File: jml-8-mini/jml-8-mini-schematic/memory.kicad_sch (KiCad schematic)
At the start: 2 parts, among them U2 28HC64, U3 60L256

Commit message: lots of updates to schematic to make pcb routing easier, start on pcb design
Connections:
- net A13: now also U3.26 (NC); no longer U3.28 (VCC)
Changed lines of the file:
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@@
     (pin "25")
+    (pin "26")
     (pin "26")
     (pin "27")
     (pin "28")
-    (pin "28")
     (pin "3")

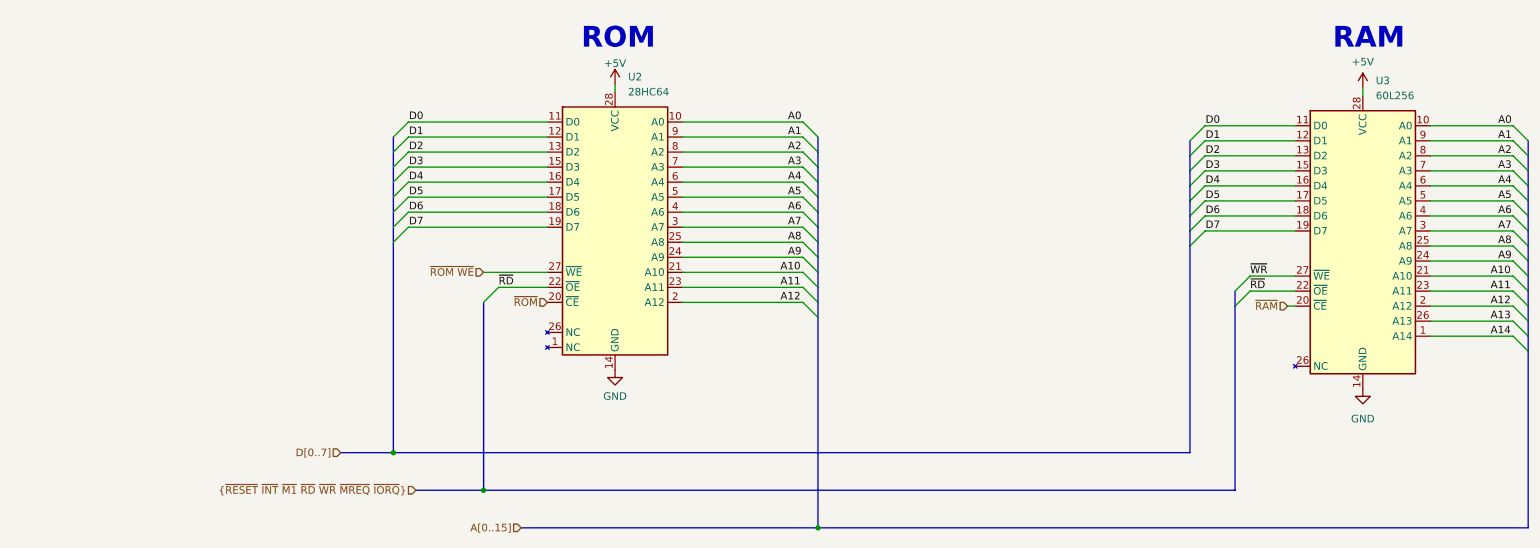
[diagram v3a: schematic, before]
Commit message: fix some errors in schematic/pcb
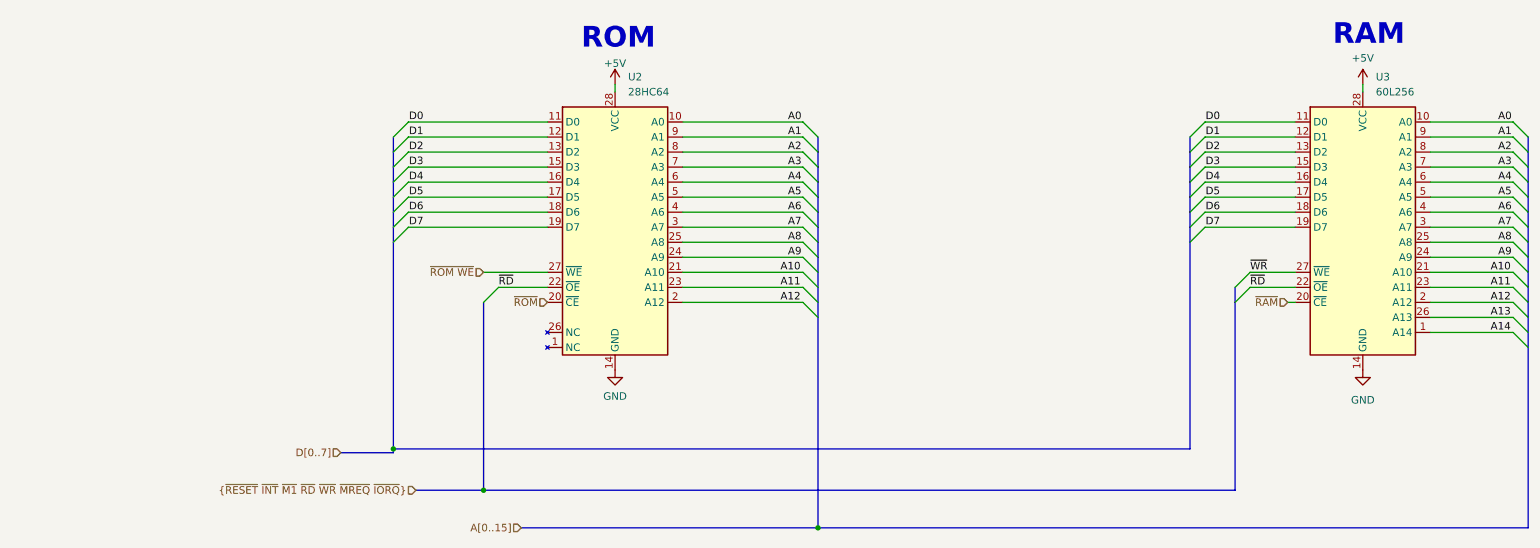
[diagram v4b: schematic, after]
